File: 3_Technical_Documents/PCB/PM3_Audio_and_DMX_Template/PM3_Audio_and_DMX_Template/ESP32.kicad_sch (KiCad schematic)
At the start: 11 parts, among them SW1 SW_DPDT_x2, SW3 SW_Push, U14 ESP32-MINI-1

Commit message: new push
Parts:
- renumbered C83 to C3, C84 to C4, C25 to C5, C27 to C6, R53 to R2, R56 to R3, R54 to R4, R55 to R5, SW3 to SW1, SW1 to SW2, U14 to U1
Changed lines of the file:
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@@
 		(dnp no)
 		(fields_autoplaced yes)
-		(property "Reference" "#PWR016"
+		(property "Reference" "#PWR025"
 			(at 273.05 45.72 0)
 			(effects
@@
 			(project "PM3_Audio_and_DMX"
 				(path "/1f276d59-ad9b-4e70-a842-f3b7e562eb9b/0cd82055-ce21-4aed-acf2-771a9b05e7c5"
-					(reference "#PWR016")
+					(reference "#PWR025")
 					(unit 1)
 				)
@@
 		(dnp no)
 		(fields_autoplaced yes)
-		(property "Reference" "SW3"
+		(property "Reference" "SW1"
 			(at 237.49 35.56 0)
 			(effects
@@
 			(project "PM3_Audio_and_DMX"
 				(path "/1f276d59-ad9b-4e70-a842-f3b7e562eb9b/0cd82055-ce21-4aed-acf2-771a9b05e7c5"
-					(reference "SW3")
+					(reference "SW1")
 					(unit 1)
 				)
@@
 		(on_board yes)
 		(dnp no)
-		(property "Reference" "#PWR059"
+		(property "Reference" "#PWR024"
 			(at 245.11 59.69 0)
 			(effects
@@
 			(project "PM3_Audio_and_DMX"
 				(path "/1f276d59-ad9b-4e70-a842-f3b7e562eb9b/0cd82055-ce21-4aed-acf2-771a9b05e7c5"
-					(reference "#PWR059")
+					(reference "#PWR024")
 					(unit 1)
 				)
@@
 		(on_board yes)
 		(dnp no)
-		(property "Reference" "R56"
+		(property "Reference" "R3"
 			(at 223.266 36.576 0)
 			(effects
@@
 			(project "PM3_Audio_and_DMX"
 				(path "/1f276d59-ad9b-4e70-a842-f3b7e562eb9b/0cd82055-ce21-4aed-acf2-771a9b05e7c5"
-					(reference "R56")
+					(reference "R3")
 					(unit 1)
 				)
@@
 		(dnp no)
 		(fields_autoplaced yes)
-		(property "Reference" "#PWR012"
+		(property "Reference" "#PWR020"
 			(at 110.49 54.61 0)
 			(effects
@@
 			(project ""
 				(path "/1f276d59-ad9b-4e70-a842-f3b7e562eb9b/0cd82055-ce21-4aed-acf2-771a9b05e7c5"
-					(reference "#PWR012")
+					(reference "#PWR020")
 					(unit 1)
 				)
@@
 		(dnp no)
 		(fields_autoplaced yes)
-		(property "Reference" "R53"
+		(property "Reference" "R2"
 			(at 30.48 29.21 90)
 			(effects
@@
 			(project "PM3_Audio_and_DMX"
 				(path "/1f276d59-ad9b-4e70-a842-f3b7e562eb9b/0cd82055-ce21-4aed-acf2-771a9b05e7c5"
-					(reference "R53")
+					(reference "R2")
 					(unit 1)
 				)
@@
 		(dnp no)
 		(fields_autoplaced yes)
-		(property "Reference" "#PWR014"
+		(property "Reference" "#PWR018"
 			(at 21.59 29.21 0)
 			(effects
@@
 			(project "PM3_Audio_and_DMX"
 				(path "/1f276d59-ad9b-4e70-a842-f3b7e562eb9b/0cd82055-ce21-4aed-acf2-771a9b05e7c5"
-					(reference "#PWR014")
+					(reference "#PWR018")
 					(unit 1)
 				)
@@
 		(on_board yes)
 		(dnp no)
-		(property "Reference" "SW1"
+		(property "Reference" "SW2"
 			(at 265.43 43.18 0)
 			(effects
@@
 			(project "PM3_Audio_and_DMX"
 				(path "/1f276d59-ad9b-4e70-a842-f3b7e562eb9b/0cd82055-ce21-4aed-acf2-771a9b05e7c5"
-					(reference "SW1")
+					(reference "SW2")
 					(unit 1)
 				)
@@
 		(dnp no)
 		(fields_autoplaced yes)
-		(property "Reference" "U14"
+		(property "Reference" "U1"
 			(at 139.3033 50.8 0)
 			(effects
@@
 			(project ""
 				(path "/1f276d59-ad9b-4e70-a842-f3b7e562eb9b/0cd82055-ce21-4aed-acf2-771a9b05e7c5"
-					(reference "U14")
+					(reference "U1")
 					(unit 1)
 				)
@@
 		(dnp no)
 		(fields_autoplaced yes)
-		(property "Reference" "C84"
+		(property "Reference" "C4"
 			(at 114.3 41.9099 0)
 			(effects
@@
 			(project "PM3_Audio_and_DMX"
 				(path "/1f276d59-ad9b-4e70-a842-f3b7e562eb9b/0cd82055-ce21-4aed-acf2-771a9b05e7c5"
-					(reference "C84")
+					(reference "C4")
 					(unit 1)
 				)
@@
 		(on_board yes)
 		(dnp no)
-		(property "Reference" "C27"
+		(property "Reference" "C6"
 			(at 221.234 46.99 0)
 			(effects
@@
 			(project "PM3_Audio_and_DMX"
 				(path "/1f276d59-ad9b-4e70-a842-f3b7e562eb9b/0cd82055-ce21-4aed-acf2-771a9b05e7c5"
-					(reference "C27")
+					(reference "C6")
 					(unit 1)
 				)
@@
 		(dnp no)
 		(fields_autoplaced yes)
-		(property "Reference" "C83"
+		(property "Reference" "C3"
 			(at 102.87 41.9099 0)
 			(effects
@@
 			(project "PM3_Audio_and_DMX"
 				(path "/1f276d59-ad9b-4e70-a842-f3b7e562eb9b/0cd82055-ce21-4aed-acf2-771a9b05e7c5"
-					(reference "C83")
+					(reference "C3")
 					(unit 1)
 				)
@@
 		(dnp no)
 		(fields_autoplaced yes)
-		(property "Reference" "#PWR08"
+		(property "Reference" "#PWR019"
 			(at 99.06 54.61 0)
 			(effects
@@
 			(project "PM3_Audio_and_DMX"
 				(path "/1f276d59-ad9b-4e70-a842-f3b7e562eb9b/0cd82055-ce21-4aed-acf2-771a9b05e7c5"
-					(reference "#PWR08")
+					(reference "#PWR019")
 					(unit 1)
 				)
@@
 		(dnp no)
 		(fields_autoplaced yes)
-		(property "Reference" "R55"
+		(property "Reference" "R5"
 			(at 255.27 58.42 90)
 			(effects
@@
 			(project "PM3_Audio_and_DMX"
 				(path "/1f276d59-ad9b-4e70-a842-f3b7e562eb9b/0cd82055-ce21-4aed-acf2-771a9b05e7c5"
-					(reference "R55")
+					(reference "R5")
 					(unit 1)
 				)
@@
 		(dnp no)
 		(fields_autoplaced yes)
-		(property "Reference" "#PWR017"
+		(property "Reference" "#PWR026"
 			(at 273.05 76.2 0)
 			(effects
@@
 			(project "PM3_Audio_and_DMX"
 				(path "/1f276d59-ad9b-4e70-a842-f3b7e562eb9b/0cd82055-ce21-4aed-acf2-771a9b05e7c5"
-					(reference "#PWR017")
+					(reference "#PWR026")
 					(unit 1)
 				)
@@
 		(on_board yes)
 		(dnp no)
-		(property "Reference" "#PWR058"
+		(property "Reference" "#PWR023"
 			(at 228.6 59.69 0)
 			(effects
@@
 			(project "PM3_Audio_and_DMX"
 				(path "/1f276d59-ad9b-4e70-a842-f3b7e562eb9b/0cd82055-ce21-4aed-acf2-771a9b05e7c5"
-					(reference "#PWR058")
+					(reference "#PWR023")
 					(unit 1)
 				)
@@
 		(on_board yes)
 		(dnp no)
-		(property "Reference" "SW1"
+		(property "Reference" "SW2"
 			(at 265.43 55.88 0)
 			(effects
@@
 			(project "PM3_Audio_and_DMX"
 				(path "/1f276d59-ad9b-4e70-a842-f3b7e562eb9b/0cd82055-ce21-4aed-acf2-771a9b05e7c5"
-					(reference "SW1")
+					(reference "SW2")
 					(unit 2)
 				)
@@
 		(dnp no)
 		(fields_autoplaced yes)
-		(property "Reference" "C25"
+		(property "Reference" "C5"
 			(at 128.27 41.9099 0)
 			(effects
@@
 			(project "PM3_Audio_and_DMX"
 				(path "/1f276d59-ad9b-4e70-a842-f3b7e562eb9b/0cd82055-ce21-4aed-acf2-771a9b05e7c5"
-					(reference "C25")
+					(reference "C5")
 					(unit 1)
 				)
@@
 		(dnp no)
 		(fields_autoplaced yes)
-		(property "Reference" "#PWR013"
+		(property "Reference" "#PWR021"
 			(at 124.46 54.61 0)
 			(effects
@@
 			(project "PM3_Audio_and_DMX"
 				(path "/1f276d59-ad9b-4e70-a842-f3b7e562eb9b/0cd82055-ce21-4aed-acf2-771a9b05e7c5"
-					(reference "#PWR013")
+					(reference "#PWR021")
 					(unit 1)
 				)
@@
 		(dnp no)
 		(fields_autoplaced yes)
-		(property "Reference" "#PWR015"
+		(property "Reference" "#PWR022"
 			(at 137.16 121.92 0)
 			(effects
@@
 			(project "PM3_Audio_and_DMX"
 				(path "/1f276d59-ad9b-4e70-a842-f3b7e562eb9b/0cd82055-ce21-4aed-acf2-771a9b05e7c5"
-					(reference "#PWR015")
+					(reference "#PWR022")
 					(unit 1)
 				)
@@
 		(dnp no)
 		(fields_autoplaced yes)
-		(property "Reference" "R54"
+		(property "Reference" "R4"
 			(at 255.27 27.94 90)
 			(effects
@@
 			(project "PM3_Audio_and_DMX"
 				(path "/1f276d59-ad9b-4e70-a842-f3b7e562eb9b/0cd82055-ce21-4aed-acf2-771a9b05e7c5"
-					(reference "R54")
-					(unit 1)
-				)
+					(reference "R4")
+					(unit 1)
+				)

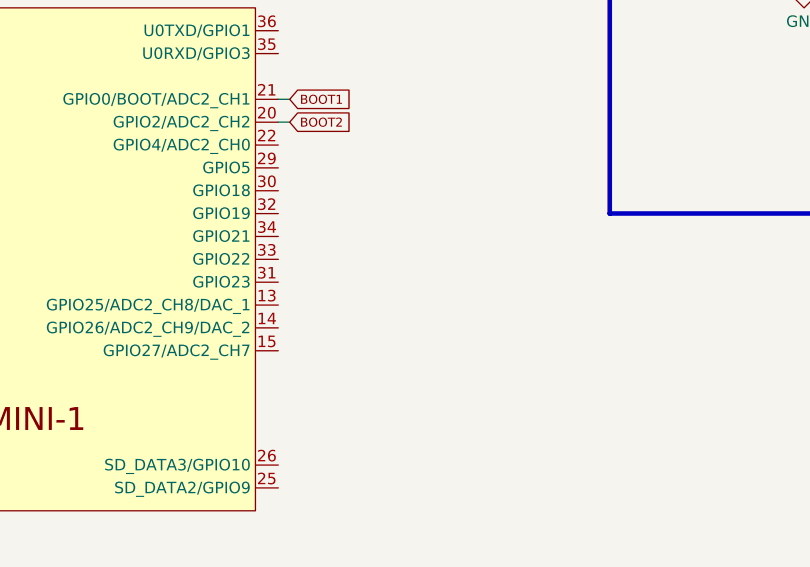
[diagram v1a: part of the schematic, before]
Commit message: i2s added
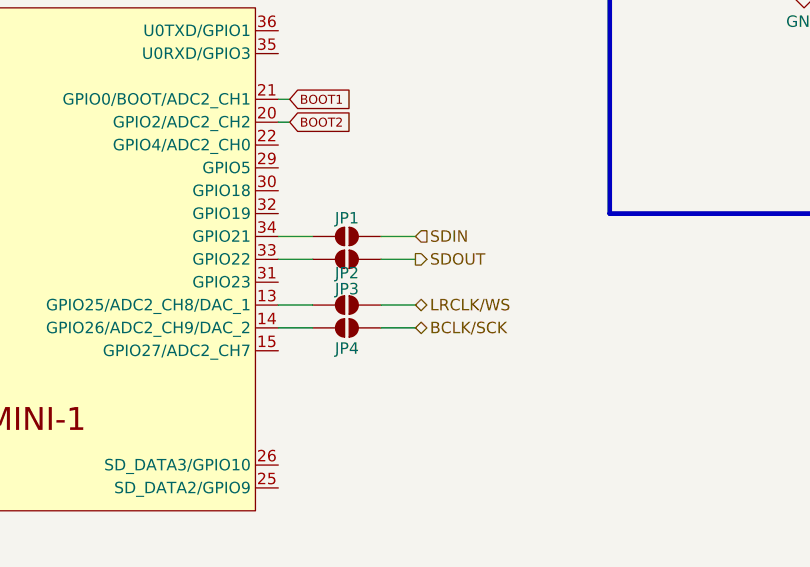
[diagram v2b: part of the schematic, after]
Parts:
- added JP1, JP2, JP3, JP4: SolderJumper_2_Open, symbol Jumper:SolderJumper_2_Open
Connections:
- net at U1.13 (GPIO25/ADC2_CH8/DAC_1): now also JP3.1 (A)
- net at U1.14 (GPIO26/ADC2_CH9/DAC_2): now also JP4.1 (A)
- net at U1.33 (GPIO22): now also JP2.1 (A)
- net at U1.34 (GPIO21): now also JP1.1 (A)
- new net BCLK/SCK: JP4.2 (B)
- new net LRCLK/WS: JP3.2 (B)
- new net SDIN: JP1.2 (B)
- new net SDOUT: JP2.2 (B)

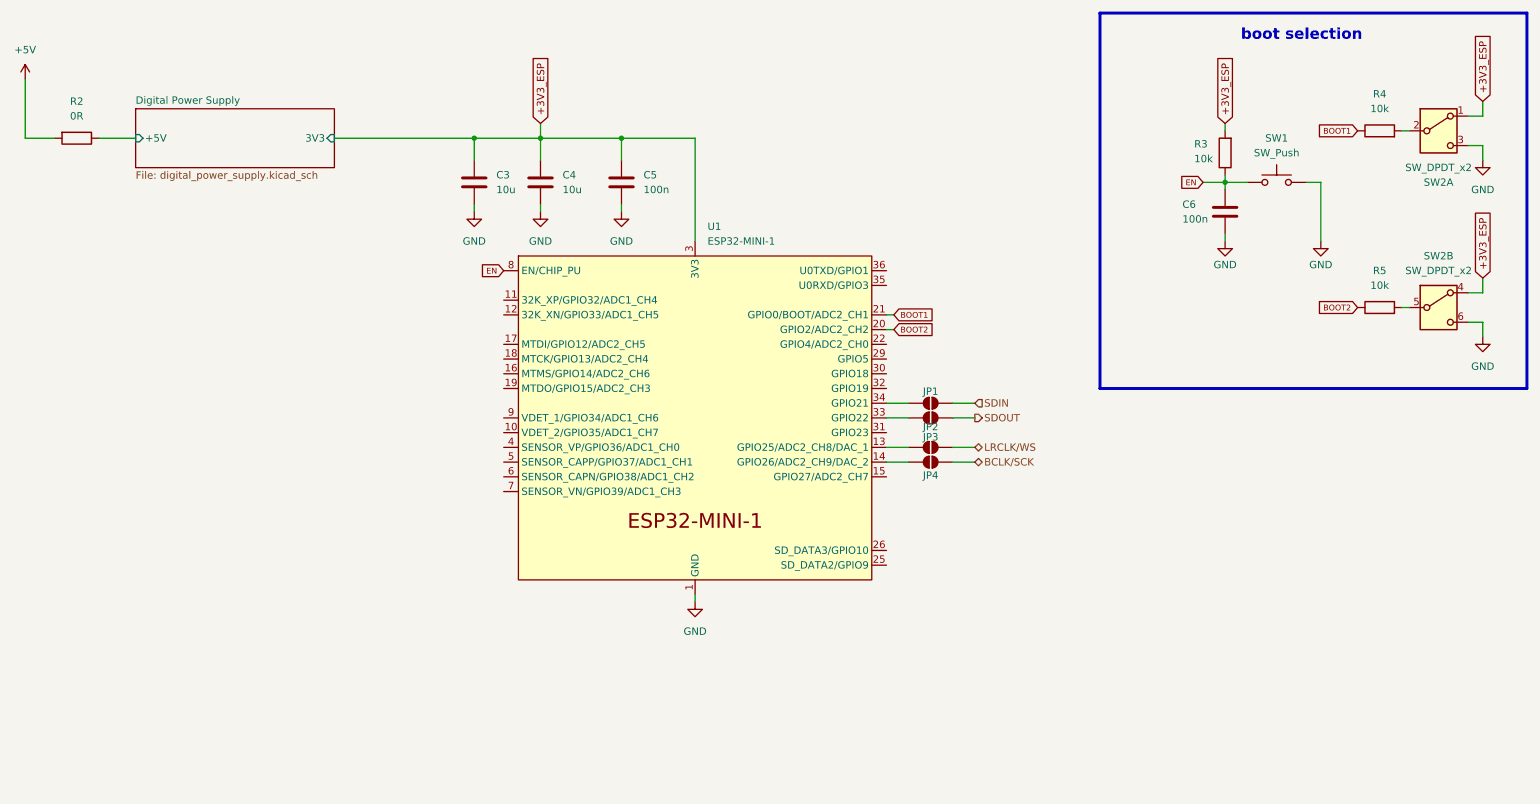
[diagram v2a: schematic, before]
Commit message: rework esp32, codec and layout
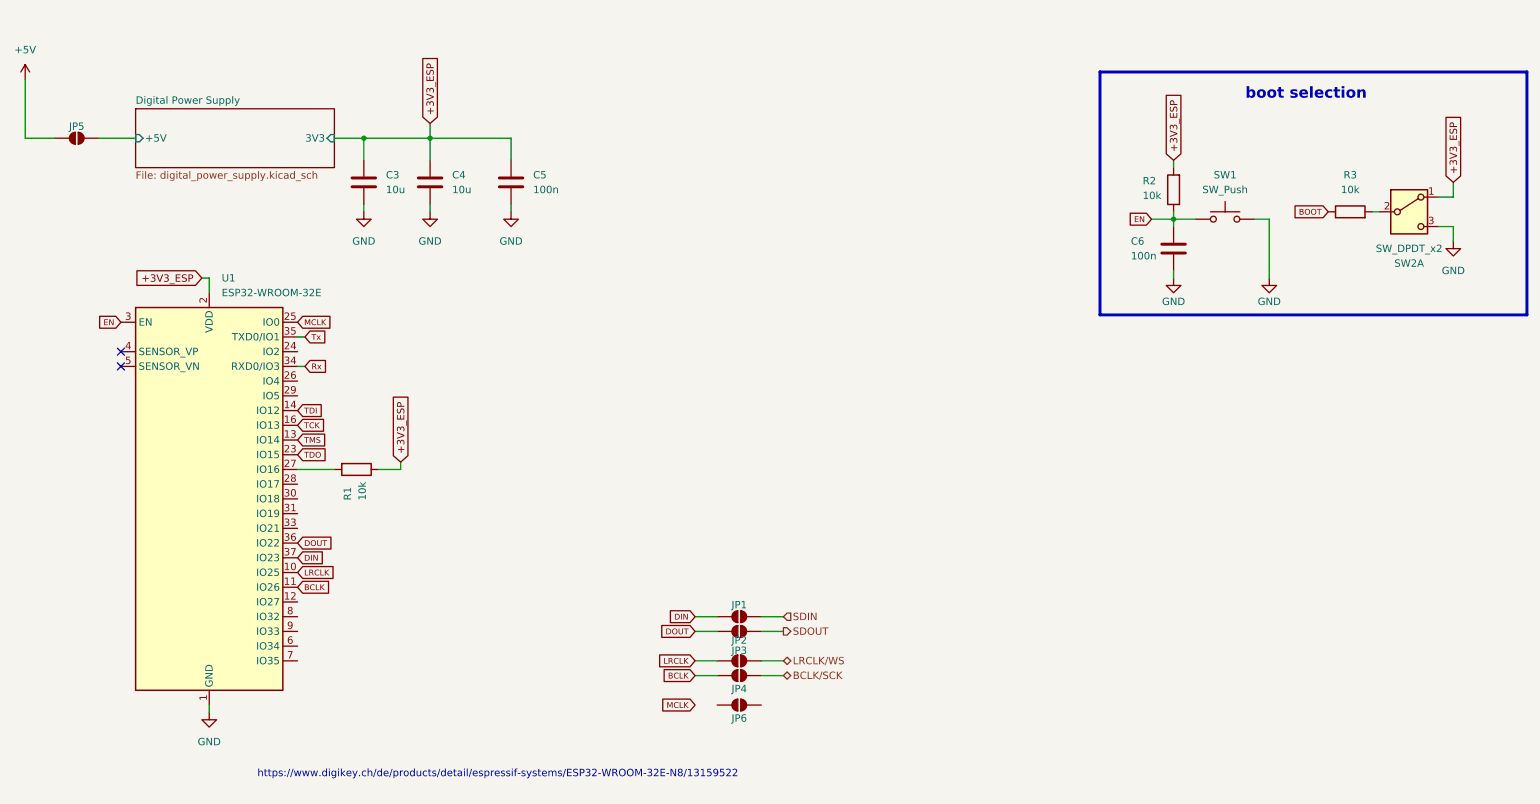
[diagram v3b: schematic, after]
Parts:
- removed R2: 0R, Resistor_SMD:R_0603_1608Metric, symbol Device:R
- removed R5: 10k, Resistor_SMD:R_0603_1608Metric, symbol Device:R
- removed unit 2 of SW2
- removed U1: ESP32-MINI-1, PCM_Espressif:ESP32-MINI-1, symbol PCM_Espressif:ESP32-MINI-1
- added JP5, JP6: SolderJumper_2_Open, symbol Jumper:SolderJumper_2_Open
- added R1: 10k, Resistor_SMD:R_0603_1608Metric, symbol Device:R
- added U1: ESP32-WROOM-32E, RF_Module:ESP32-WROOM-32D, symbol RF_Module:ESP32-WROOM-32E
- renumbered R3 to R2, R4 to R3
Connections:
- net +3V3_ESP: now also R1.1, U1.2 (VDD)
- net +5V: now also JP5.1 (A)
- net Digital Power Supply/+5V: now also JP5.2 (B)
- net EN: now also U1.3 (EN)
- net GND: now also U1.1 (GND), U1.15 (GND), U1.38 (GND), U1.39 (GND)
- net LRCLK: now reaches JP3.1 (A)
- net LRCLK: now also U1.10 (IO25)
- net BCLK: now reaches JP4.1 (A)
- net BCLK: now also U1.11 (IO26)
- net DOUT: now reaches JP2.1 (A)
- net DOUT: now also U1.36 (IO22)
- net DIN: now reaches JP1.1 (A)
- net DIN: now also U1.37 (IO23)
- net BOOT1 renamed BOOT
- new net: R1.2, U1.27 (IO16)
- new net MCLK: U1.25 (IO0)
- new net Rx: U1.34 (RXD0/IO3)
- new net TCK: U1.16 (IO13)
- new net TDI: U1.14 (IO12)
- new net TDO: U1.23 (IO15)
- new net TMS: U1.13 (IO14)
- new net Tx: U1.35 (TXD0/IO1)
- no-connect marks 0 -> 2
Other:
- note added: "https://www.digikey.ch/de/products/detail/espressif-systems/ESP32-WROOM-32E-N8/13159522"
- moved on the sheet: C3, C4, C5, C6, JP1, JP2, JP3, JP4, R2, R3, SW1, SW2A

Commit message: minor modifications to esp32 bootmodes
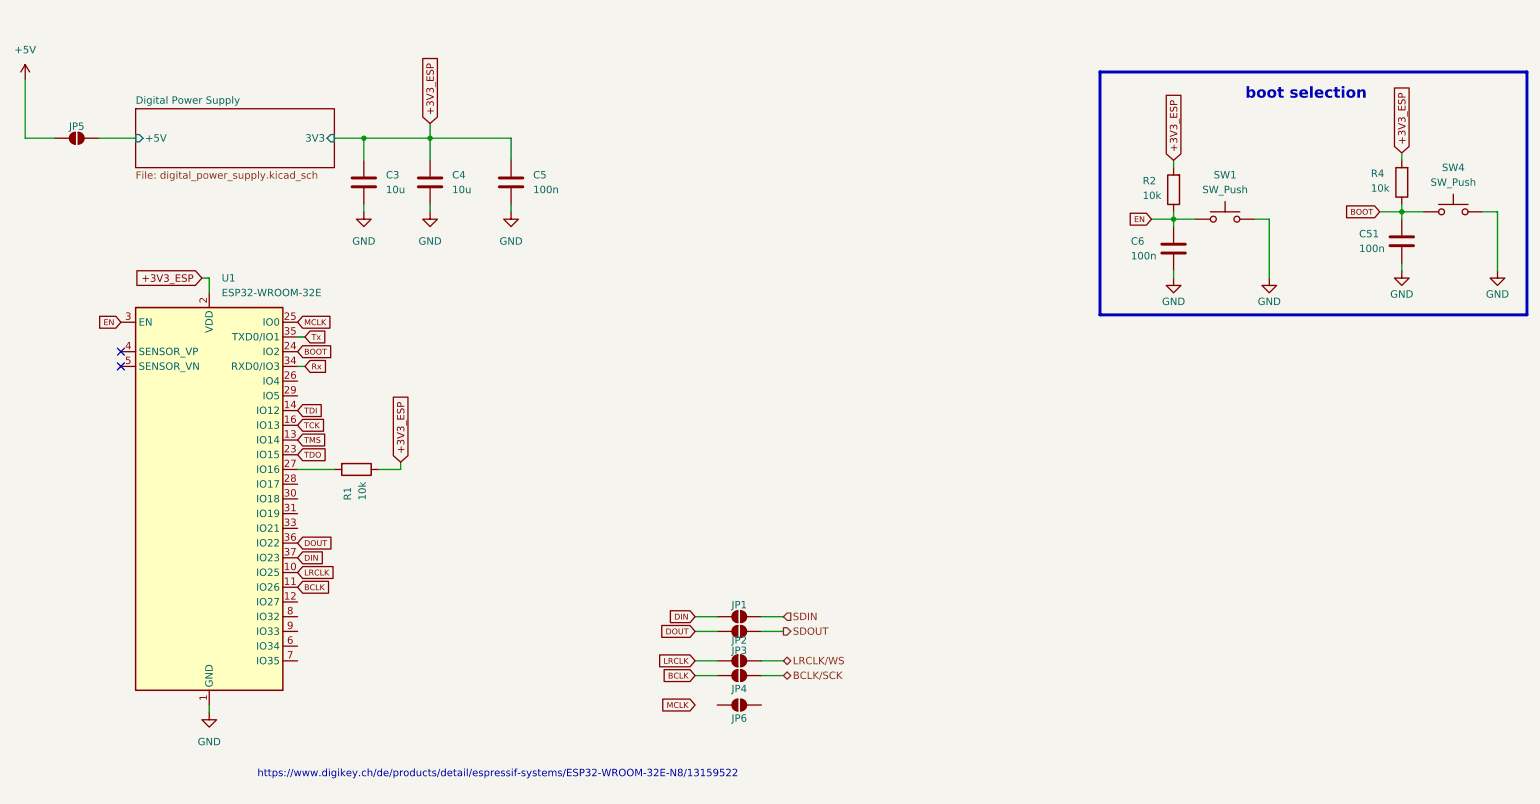
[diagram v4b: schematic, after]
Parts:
- removed R3: 10k, Resistor_SMD:R_0603_1608Metric, symbol Device:R
- removed SW2: SW_DPDT_x2, Button_Switch_SMD:SW_DPDT_CK_JS202011JCQN, symbol Switch:SW_DPDT_x2
- added C51: 100n, Capacitor_SMD:C_0603_1608Metric, symbol Device:C
- added R4: 10k, Resistor_SMD:R_0603_1608Metric, symbol Device:R
- added SW4: SW_Push, Button_Switch_SMD:SW_SPST_TL3342, symbol Switch:SW_Push
- SW1: footprint (none) -> Button_Switch_SMD:SW_SPST_TL3342
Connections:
- net +3V3_ESP: now also R4.2
- net BOOT: now also U1.24 (IO2), C51.1, R4.1, SW4.2
- net GND: now also C51.2, SW4.1

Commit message: esp-stm connection (+ conflict recolution)
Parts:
- removed C51: 100n, Capacitor_SMD:C_0603_1608Metric, symbol Device:C
- removed R4: 10k, Resistor_SMD:R_0603_1608Metric, symbol Device:R
- removed SW4: SW_Push, Button_Switch_SMD:SW_SPST_TL3342, symbol Switch:SW_Push
- added C50: 100n, Capacitor_SMD:C_0603_1608Metric, symbol Device:C
- added JP10, JP7, JP8, JP9: SolderJumper_2_Open, Jumper:SolderJumper-2_P1.3mm_Open_RoundedPad1.0x1.5mm, symbol Jumper:SolderJumper_2_Open
- added R3: 10k, Resistor_SMD:R_0603_1608Metric, symbol Device:R
- added SW2: SW_Push, Button_Switch_SMD:SW_SPST_TL3342, symbol Switch:SW_Push
- JP1, JP2, JP3, JP4, JP5, JP6: footprint (none) -> Jumper:SolderJumper-2_P1.3mm_Open_RoundedPad1.0x1.5mm
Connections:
- net +3V3_ESP: now also R3.2
- net BOOT: now also U1.25 (IO0), C50.1, R3.1, SW2.2; no longer U1.24 (IO2)
- net GND: now also C50.2, SW2.1
- net MCLK: now also JP6.2 (B); no longer U1.25 (IO0)
- net MCLK_ESP: now reaches JP6.1 (A)
- net MCLK_ESP: now also U1.28 (IO17)
- net UART_TX: now reaches U1.12 (IO27)
- net LRCLK_2: now reaches U1.30 (IO18)
- net LRCLK_2: now also JP9.1 (A)
- net BCLK_2: now reaches U1.31 (IO19)
- net BCLK_2: now also JP10.1 (A)
- net UART_RX: now reaches U1.33 (IO21)
- net DOUT_2: now reaches U1.8 (IO32)
- net DOUT_2: now also JP8.1 (A)
- net DIN_2: now reaches U1.9 (IO33)
- net DIN_2: now also JP7.1 (A)
- net BCLK renamed BCLK_1
- net BCLK/SCK renamed BCLK/SCK_1
- net DIN renamed DIN_1
- net DOUT renamed DOUT_1
- net LRCLK renamed LRCLK_1
- net LRCLK/WS renamed LRCLK/WS_1
- net SDIN renamed SDIN_1
- net SDOUT renamed SDOUT_1
- new net BCLK/SCK_2: JP10.2 (B)
- new net LRCLK/WS_2: JP9.2 (B)
- new net SDIN_2: JP7.2 (B)
- new net SDOUT_2: JP8.2 (B)
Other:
- note added: "I2S (2 Interfaces)"
- moved on the sheet: JP1, JP2, JP3, JP4, JP6, R1
